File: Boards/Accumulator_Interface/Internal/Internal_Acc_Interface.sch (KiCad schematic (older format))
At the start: 6 parts, among them J1 MM_F_VT_14, J2 SS-126-G-2, J3 BBS-126-G-A, J4 MM_F_VT_16, J5 MicroFit_VT_4, U1 MicroFit_VT_6

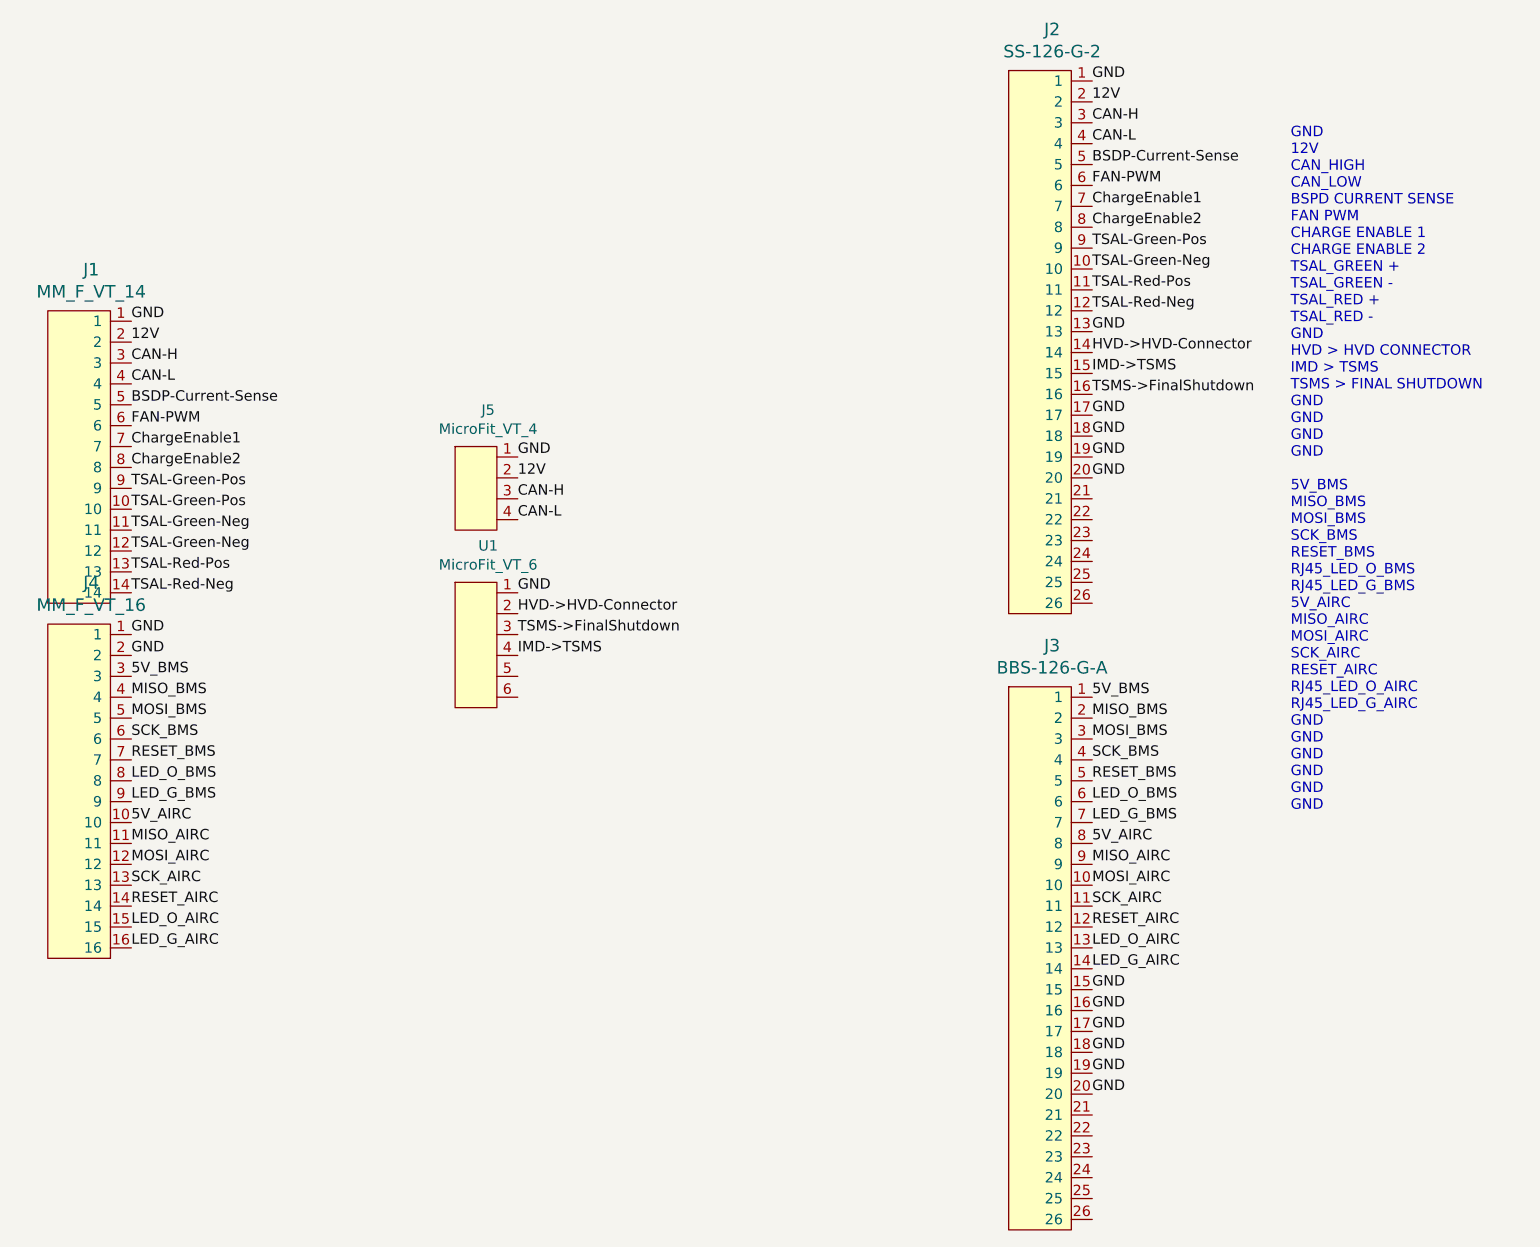
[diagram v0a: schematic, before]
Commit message: first pass of acc interface and rev1.1 of periph layout
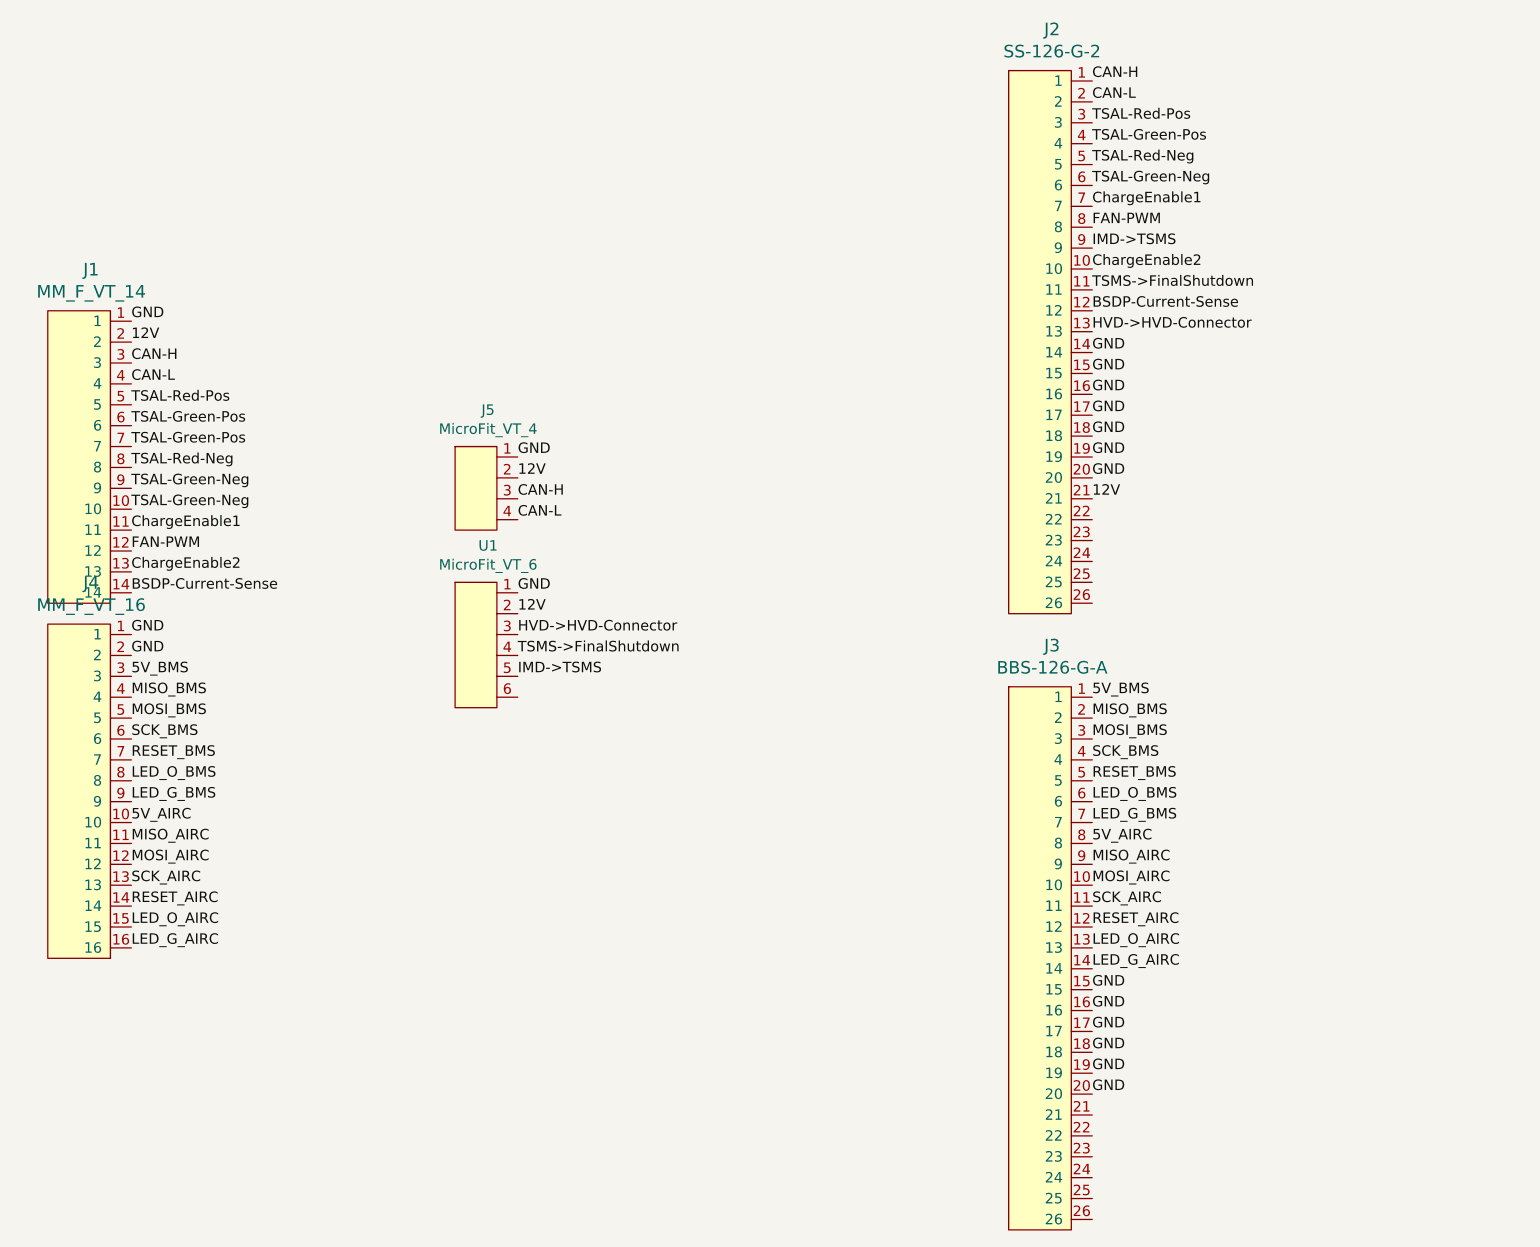
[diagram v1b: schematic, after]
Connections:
- net 12V: now also J2.21, U1.2; no longer J2.2
- net BSDP-Current-Sense: now also J1.14, J2.12; no longer J1.5, J2.5
- net CAN-H: now also J2.1; no longer J2.3
- net CAN-L: now also J2.2; no longer J2.4
- net ChargeEnable1: now also J1.11; no longer J1.7
- net ChargeEnable2: now also J1.13, J2.10; no longer J1.8, J2.8
- net FAN-PWM: now also J1.12, J2.8; no longer J1.6, J2.6
- net GND: now also J2.14, J2.15, J2.16; no longer J2.1, J2.13
- net HVD->HVD-Connector: now also J2.13, U1.3; no longer J2.14, U1.2
- net IMD->TSMS: now also J2.9, U1.5; no longer J2.15, U1.4
- net TSAL-Green-Neg: now also J1.10, J1.9, J2.6; no longer J1.11, J1.12, J2.10
- net TSAL-Green-Pos: now also J1.6, J1.7, J2.4; no longer J1.10, J1.9, J2.9
- net TSAL-Red-Neg: now also J1.8, J2.5; no longer J1.14, J2.12
- net TSAL-Red-Pos: now also J1.5, J2.3; no longer J1.13, J2.11
- net TSMS->FinalShutdown: now also J2.11, U1.4; no longer J2.16, U1.3
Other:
- note removed: "GND\n12V\nCAN_HIGH\nCAN_LOW\nBSPD CURRENT SENSE\nFAN PWM\nCHARGE ENABLE 1\nCHARGE ENABLE 2\nTSAL_GREEN +\nTSAL_GREEN -\nTSAL_RED +\nTSAL_RED -\nGND\nHVD > HVD CONNECTOR\nIMD > TSMS\nTSMS > FINAL SHUTDOWN\nGND\nGND\nGND\nGND\n\n5V_BMS\nMISO_BMS\nMOSI_BMS\nSCK_BMS\nRESET_BMS\nRJ45_LED_O_BMS\nRJ45_LED_G_BMS\n5V_AIRC\nMISO_AIRC\nMOSI_AIRC\nSCK_AIRC\nRESET_AIRC\nRJ45_LED_O_AIRC\nRJ45_LED_G_AIRC\nGND\n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"
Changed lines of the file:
@@
 	1    0    0    -1
 $EndComp
+Text Label 9050 2650 0    50   ~ 0
+GND
+Text Label 9050 2750 0    50   ~ 0
+12V
 Text Label 9050 750  0    50   ~ 0
-GND
+CAN-H
 Text Label 9050 850  0    50   ~ 0
-12V
-Text Label 9050 950  0    50   ~ 0
-CAN-H
-Text Label 9050 1050 0    50   ~ 0
 CAN-L
-Text Label 9050 1150 0    50   ~ 0
+Text Label 9050 1850 0    50   ~ 0
 BSDP-Current-Sense
-Text Label 9050 1250 0    50   ~ 0
+Text Label 9050 1450 0    50   ~ 0
 FAN-PWM
 Text Label 9050 1350 0    50   ~ 0
 ChargeEnable1
-Text Label 9050 1450 0    50   ~ 0
+Text Label 9050 1650 0    50   ~ 0
 ChargeEnable2
+Text Label 9050 1050 0    50   ~ 0
+TSAL-Green-Pos
+Text Label 9050 1250 0    50   ~ 0
+TSAL-Green-Neg
+Text Label 9050 950  0    50   ~ 0
+TSAL-Red-Pos
+Text Label 9050 1150 0    50   ~ 0
+TSAL-Red-Neg
+Text Label 9050 2150 0    50   ~ 0
+GND
+Text Label 9050 1950 0    50   ~ 0
+HVD->HVD-Connector
 Text Label 9050 1550 0    50   ~ 0
-TSAL-Green-Pos
-Text Label 9050 1650 0    50   ~ 0
-TSAL-Green-Neg
+IMD->TSMS
 Text Label 9050 1750 0    50   ~ 0
-TSAL-Red-Pos
-Text Label 9050 1850 0    50   ~ 0
-TSAL-Red-Neg
-Text Label 9050 1950 0    50   ~ 0
-GND
-Text Label 9050 2050 0    50   ~ 0
-HVD->HVD-Connector
-Text Label 9050 2150 0    50   ~ 0
-IMD->TSMS
+TSMS->FinalShutdown
 Text Label 9050 2250 0    50   ~ 0
-TSMS->FinalShutdown
+GND
 Text Label 9050 2350 0    50   ~ 0
 GND
@@
 GND
 Text Label 9050 2550 0    50   ~ 0
-GND
-Text Label 9050 2650 0    50   ~ 0
 GND
 Text Label 9050 3700 0    50   ~ 0
@@
 Text Label 9050 5600 0    50   ~ 0
 GND
-Text Notes 10000 4250 0    50   ~ 0
-GND\n12V\nCAN_HIGH\nCAN_LOW\nBSPD CURRENT SENSE\nFAN PWM\nCHARGE ENABLE 1\nCHARGE ENABLE 2\nTSAL_GREEN +\nTSAL_GREEN -\nTSAL_RED +\nTSAL_RED -\nGND\nHVD > HVD CONNECTOR\nIMD > TSMS\nTSMS > FINAL SHUTDOWN\nGND\nGND\nGND\nGND\n\n5V_BMS\nMISO_BMS\nMOSI_BMS\nSCK_BMS\nRESET_BMS\nRJ45_LED_O_BMS\nRJ45_LED_G_BMS\n5V_AIRC\nMISO_AIRC\nMOSI_AIRC\nSCK_AIRC\nRESET_AIRC\nRJ45_LED_O_AIRC\nRJ45_LED_G_AIRC\nGND\nGND\nGND\nGND\nGND\nGND
 $Comp
 L formula:MM_F_VT_14 J1
@@
 	1    0    0    -1
 $EndComp
-Text Label 4450 1900 0    50   ~ 0
-GND
-Text Label 4450 2000 0    50   ~ 0
-12V
-Text Label 4450 2100 0    50   ~ 0
-CAN-H
-Text Label 4450 2200 0    50   ~ 0
-CAN-L
-Text Label 4450 2300 0    50   ~ 0
-BSDP-Current-Sense
-Text Label 4450 2400 0    50   ~ 0
-FAN-PWM
-Text Label 4450 2500 0    50   ~ 0
-ChargeEnable1
-Text Label 4450 2600 0    50   ~ 0
-ChargeEnable2
-Text Label 4450 2700 0    50   ~ 0
-TSAL-Green-Pos
-Text Label 4450 2900 0    50   ~ 0
-TSAL-Green-Neg
-Text Label 4450 3100 0    50   ~ 0
-TSAL-Red-Pos
-Text Label 4450 3200 0    50   ~ 0
-TSAL-Red-Neg
 Text Label 4450 3600 0    50   ~ 0
 5V_BMS
@@
 Text Label 4450 4900 0    50   ~ 0
 LED_G_AIRC
-Text Label 4450 3000 0    50   ~ 0
-TSAL-Green-Neg
-Text Label 4450 2800 0    50   ~ 0
-TSAL-Green-Pos
 $Comp
 L formula:MM_F_VT_16 J4
@@
 Text Label 6300 2850 0    50   ~ 0
 CAN-L
+Text Label 6300 3400 0    50   ~ 0
+HVD->HVD-Connector
+Text Label 6300 3600 0    50   ~ 0
+IMD->TSMS
+Text Label 6300 3500 0    50   ~ 0
+TSMS->FinalShutdown
+Text Label 9050 2050 0    50   ~ 0
+GND
+Text Label 4450 2100 0    50   ~ 0
+CAN-H
+Text Label 4450 2200 0    50   ~ 0
+CAN-L
+Text Label 4450 3200 0    50   ~ 0
+BSDP-Current-Sense
+Text Label 4450 3000 0    50   ~ 0
+FAN-PWM
+Text Label 4450 2900 0    50   ~ 0
+ChargeEnable1
+Text Label 4450 3100 0    50   ~ 0
+ChargeEnable2
+Text Label 4450 2400 0    50   ~ 0
+TSAL-Green-Pos
+Text Label 4450 2700 0    50   ~ 0
+TSAL-Green-Neg
+Text Label 4450 2300 0    50   ~ 0
+TSAL-Red-Pos
+Text Label 4450 2600 0    50   ~ 0
+TSAL-Red-Neg
+Text Label 4450 1900 0    50   ~ 0
+GND
+Text Label 4450 2500 0    50   ~ 0
+TSAL-Green-Pos
+Text Label 4450 2800 0    50   ~ 0
+TSAL-Green-Neg
+Text Label 4450 2000 0    50   ~ 0
+12V
 Text Label 6300 3300 0    50   ~ 0
-HVD->HVD-Connector
-Text Label 6300 3500 0    50   ~ 0
-IMD->TSMS
-Text Label 6300 3400 0    50   ~ 0
-TSMS->FinalShutdown
+12V
 $EndSCHEMATC

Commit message: final rev interface v1
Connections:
- net 12V: now also J1.13, J2.22; no longer J1.2
- net BSDP-Current-Sense: now also J1.1; no longer J1.14
- net ChargeEnable1: now also J1.4; no longer J1.11
- net ChargeEnable2: now also J1.2; no longer J1.13
- net FAN-PWM: now also J1.3; no longer J1.12
- net GND: now also J1.14; no longer J1.1
- net TSAL-Green-Neg: now also J1.5, J1.6; no longer J1.10, J1.9
- net TSAL-Green-Pos: now also J1.8, J1.9; no longer J1.6, J1.7
- net TSAL-Red-Neg: now also J1.7; no longer J1.8
- net TSAL-Red-Pos: now also J1.10; no longer J1.5
- net CAN-H renamed CAN_P
- net CAN_P: now also J1.12; no longer J1.3
- net CAN-L renamed CAN_N
- net CAN_N: now also J1.11; no longer J1.4
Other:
- note added: "Accumulator Interface -- Internal"
- note added: "To Emeter"
- note added: "To External"
- note added: "To Megaboard"
- moved on the sheet: U1
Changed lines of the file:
@@
 12V
 Text Label 9050 750  0    50   ~ 0
-CAN-H
+CAN_P
 Text Label 9050 850  0    50   ~ 0
-CAN-L
+CAN_N
 Text Label 9050 1850 0    50   ~ 0
 BSDP-Current-Sense
@@
 L formula:MicroFit_VT_6 U1
 U 1 1 5E1FDFE4
-P 6100 3450
-F 0 "U1" H 6158 3925 50  0000 C CNN
-F 1 "MicroFit_VT_6" H 6158 3834 50  0000 C CNN
-F 2 "footprints:MicroFit_VT_6" H 6100 3050 50  0001 C CNN
-F 3 "" H 6100 3450 50  0001 C CNN
-	1    6100 3450
+P 4200 5550
+F 0 "U1" H 4258 6025 50  0000 C CNN
+F 1 "MicroFit_VT_6" H 4258 5934 50  0000 C CNN
+F 2 "footprints:MicroFit_VT_6" H 4200 5150 50  0001 C CNN
+F 3 "" H 4200 5550 50  0001 C CNN
+	1    4200 5550
 	1    0    0    -1
 $EndComp
 Text Label 6300 2550 0    50   ~ 0
 GND
-Text Label 6300 3200 0    50   ~ 0
+Text Label 4400 5300 0    50   ~ 0
 GND
 Text Label 6300 2650 0    50   ~ 0
 12V
 Text Label 6300 2750 0    50   ~ 0
-CAN-H
+CAN_P
 Text Label 6300 2850 0    50   ~ 0
-CAN-L
-Text Label 6300 3400 0    50   ~ 0
+CAN_N
+Text Label 4400 5500 0    50   ~ 0
 HVD->HVD-Connector
-Text Label 6300 3600 0    50   ~ 0
+Text Label 4400 5700 0    50   ~ 0
 IMD->TSMS
-Text Label 6300 3500 0    50   ~ 0
+Text Label 4400 5600 0    50   ~ 0
 TSMS->FinalShutdown
 Text Label 9050 2050 0    50   ~ 0
 GND
+Text Label 4450 3000 0    50   ~ 0
+CAN_P
+Text Label 4450 2900 0    50   ~ 0
+CAN_N
+Text Label 4450 1900 0    50   ~ 0
+BSDP-Current-Sense
 Text Label 4450 2100 0    50   ~ 0
-CAN-H
+FAN-PWM
 Text Label 4450 2200 0    50   ~ 0
-CAN-L
+ChargeEnable1
+Text Label 4450 2000 0    50   ~ 0
+ChargeEnable2
+Text Label 4450 2700 0    50   ~ 0
+TSAL-Green-Pos
+Text Label 4450 2400 0    50   ~ 0
+TSAL-Green-Neg
+Text Label 4450 2800 0    50   ~ 0
+TSAL-Red-Pos
+Text Label 4450 2500 0    50   ~ 0
+TSAL-Red-Neg
 Text Label 4450 3200 0    50   ~ 0
-BSDP-Current-Sense
-Text Label 4450 3000 0    50   ~ 0
-FAN-PWM
-Text Label 4450 2900 0    50   ~ 0
-ChargeEnable1
+GND
+Text Label 4450 2600 0    50   ~ 0
+TSAL-Green-Pos
+Text Label 4450 2300 0    50   ~ 0
+TSAL-Green-Neg
 Text Label 4450 3100 0    50   ~ 0
-ChargeEnable2
-Text Label 4450 2400 0    50   ~ 0
-TSAL-Green-Pos
-Text Label 4450 2700 0    50   ~ 0
-TSAL-Green-Neg
-Text Label 4450 2300 0    50   ~ 0
-TSAL-Red-Pos
-Text Label 4450 2600 0    50   ~ 0
-TSAL-Red-Neg
-Text Label 4450 1900 0    50   ~ 0
-GND
-Text Label 4450 2500 0    50   ~ 0
-TSAL-Green-Pos
-Text Label 4450 2800 0    50   ~ 0
-TSAL-Green-Neg
-Text Label 4450 2000 0    50   ~ 0
-12V
-Text Label 6300 3300 0    50   ~ 0
-12V
+12V
+Text Label 4400 5400 0    50   ~ 0
+12V
+Text Notes 3900 1450 0    118  ~ 0
+To Megaboard
+Text Notes 5800 2150 0    118  ~ 0
+To Emeter
+Text Notes 9500 3000 0    118  ~ 0
+To External
+Text Label 9050 2850 0    50   ~ 0
+12V
+Text Notes 3950 900  0    157  ~ 0
+Accumulator Interface -- Internal
 $EndSCHEMATC
